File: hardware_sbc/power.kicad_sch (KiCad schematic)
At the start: 56 parts, among them J6 Conn_01x02, J7 S2B-PH-K-S(LF)(SN), J8 Conn_01x01_Male, J9 0874380343, U10 MIC94164, U11 BQ29702, U12 BQ27426, U14 CSD85302L, U5 MP2636GR-P, U6 NCP133AMX150TCG

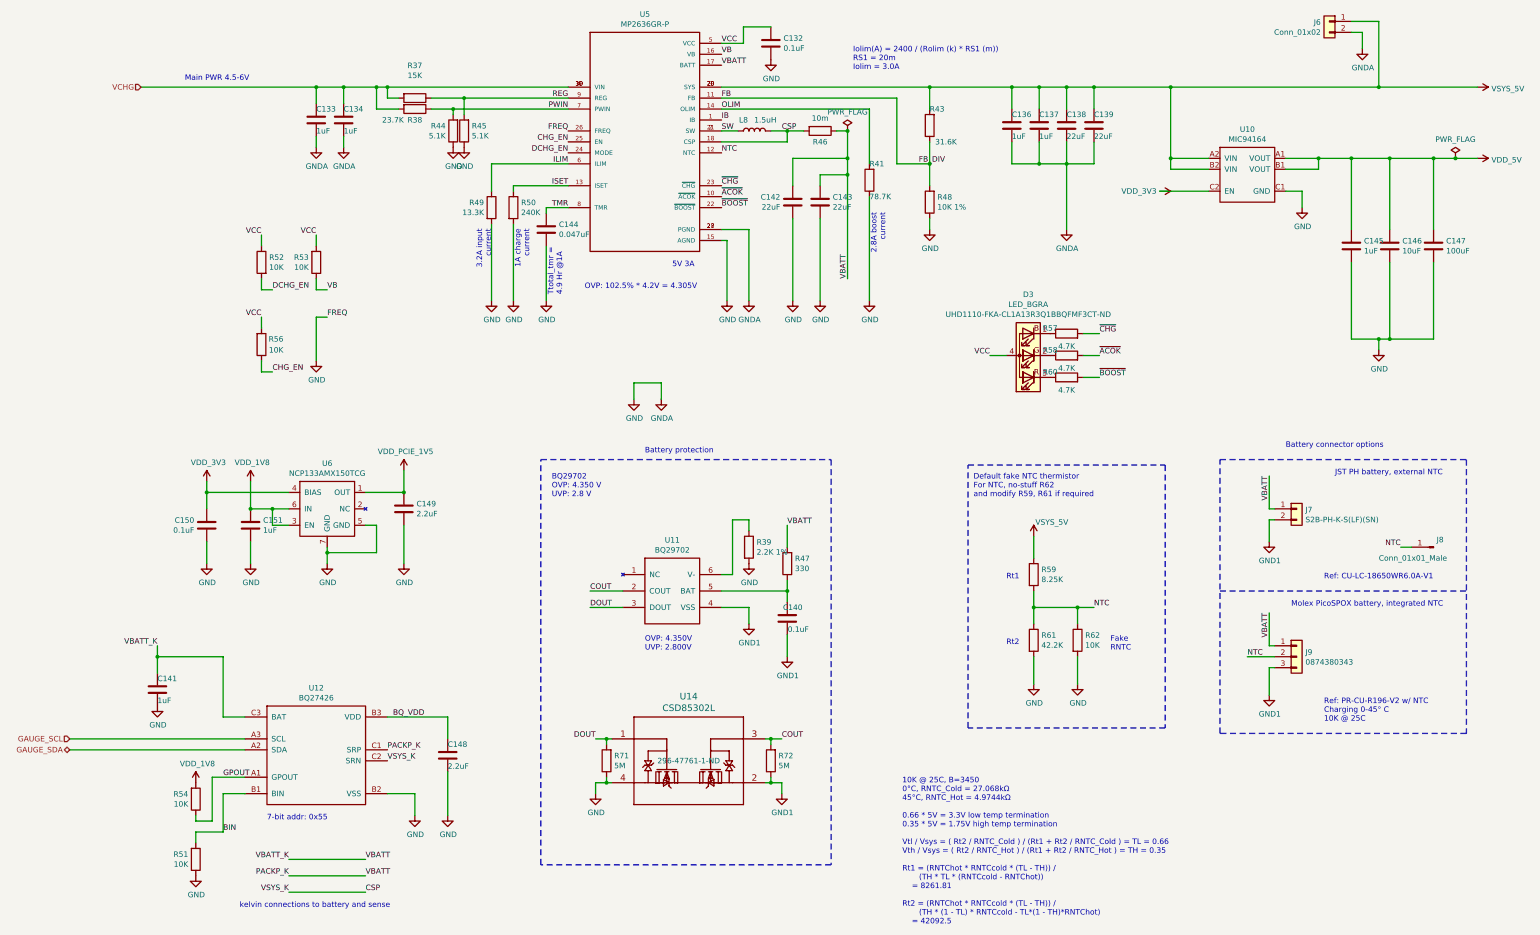
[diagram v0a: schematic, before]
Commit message: Updated production files and fixed schematic link issue.
Fixed schematic unit number issue and re-linked to PCB.
New gerbers, STEP file, schematic PDF.
Deleted old KiCAD 6 files.
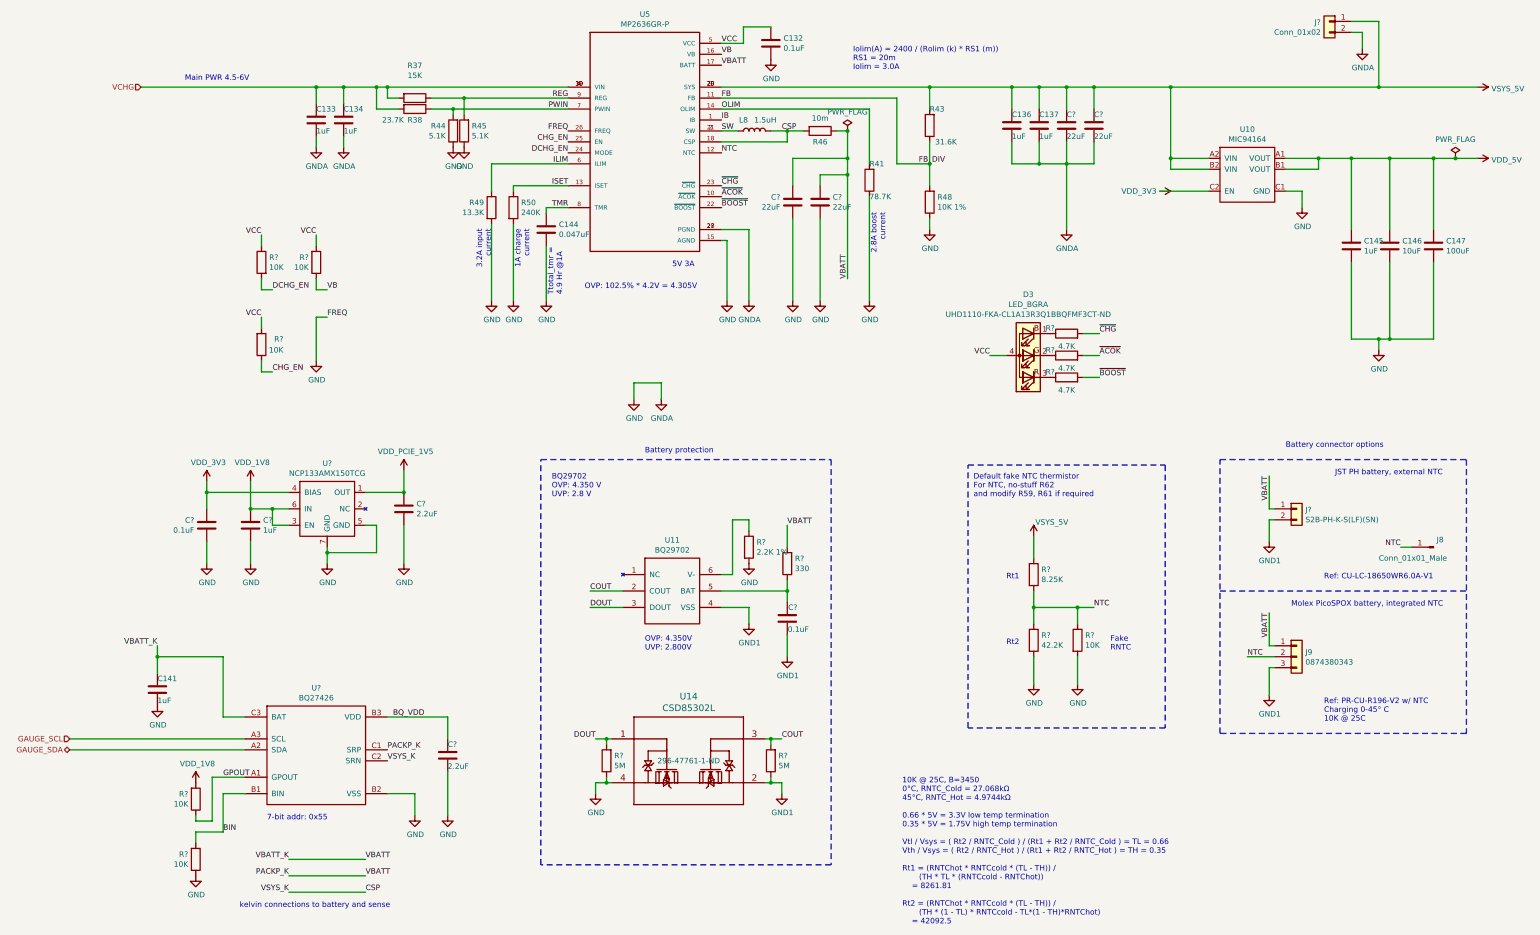
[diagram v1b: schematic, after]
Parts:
- renumbered C151 to C?, C150 to C?, C149 to C?, C142 to C?, C143 to C?, C148 to C?, C140 to C?, C138 to C?, C139 to C?, J7 to J?, J6 to J?, R56 to R?, R52 to R?, R53 to R?, R47 to R?, R39 to R?, R51 to R?, R54 to R?, R57 to R?, R58 to R?, R60 to R?, R72 to R?, R71 to R?, R59 to R?, R61 to R?, R62 to R?, U6 to U?, U12 to U?
